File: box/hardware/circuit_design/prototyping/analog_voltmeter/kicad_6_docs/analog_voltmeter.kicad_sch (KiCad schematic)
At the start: 0 parts

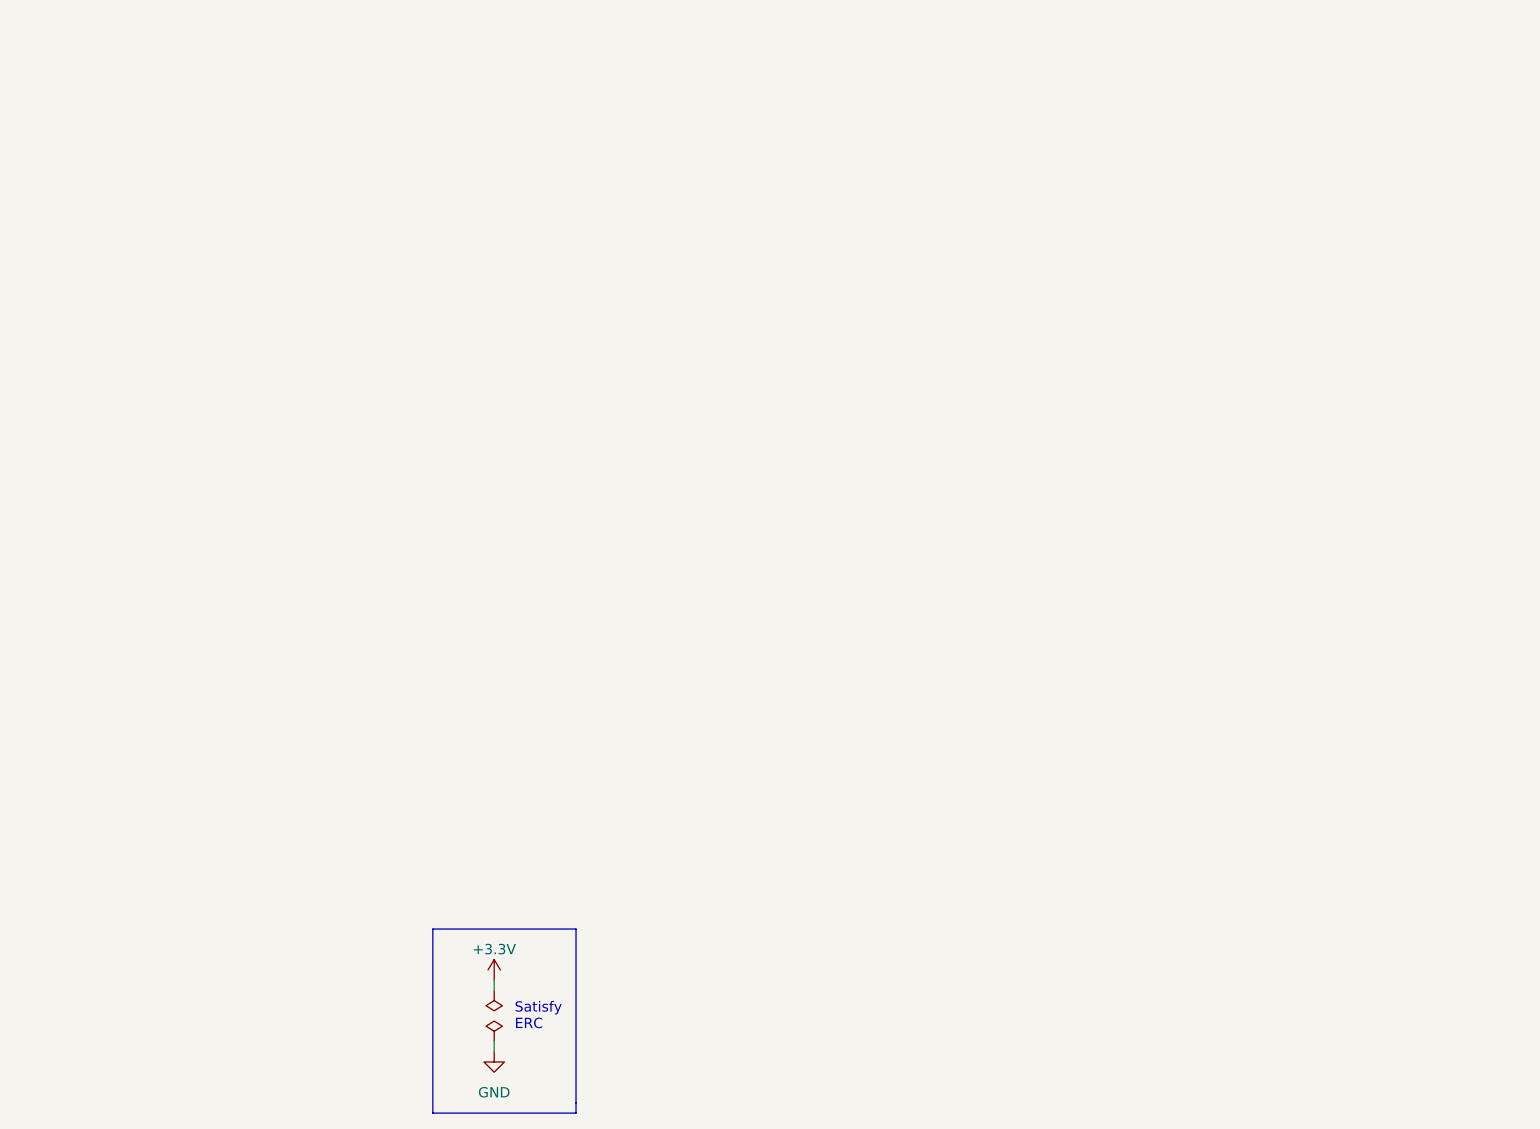
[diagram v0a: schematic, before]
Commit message: Change LED and switch breakouts, use headers instead of components
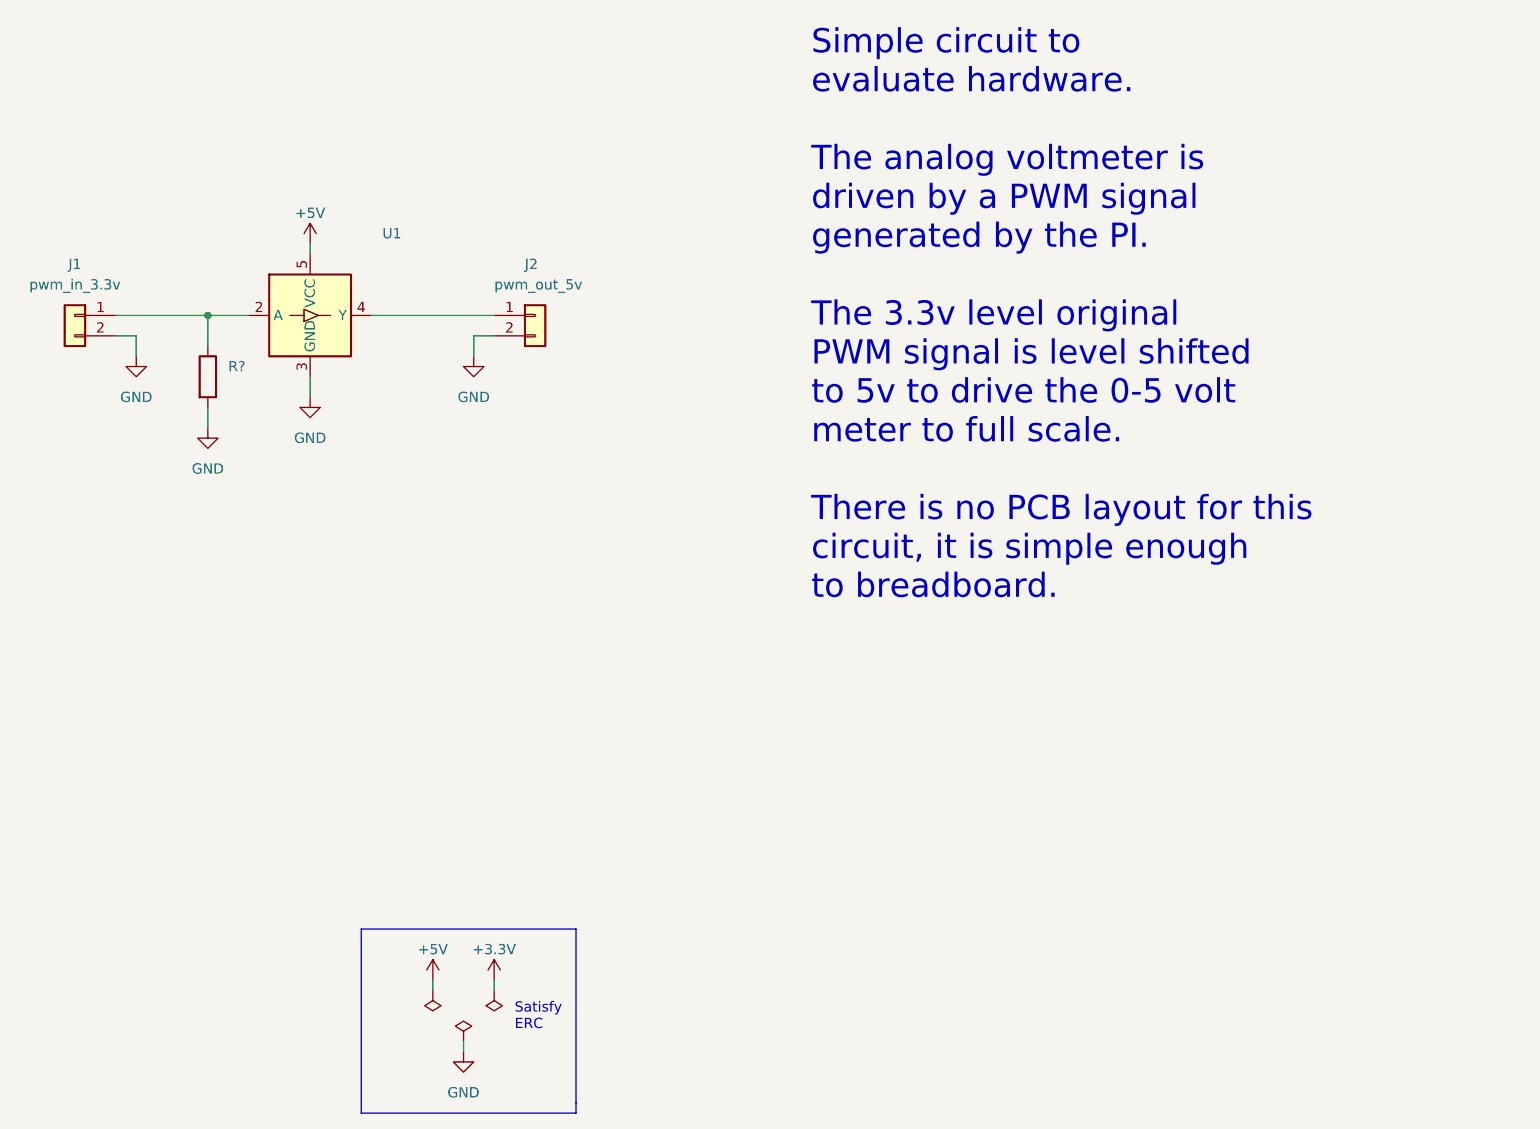
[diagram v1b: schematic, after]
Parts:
- added J1: pwm_in_3.3v, symbol Connector_Generic:Conn_01x02
- added J2: pwm_out_5v, symbol Connector_Generic:Conn_01x02
- added R?: (no value), symbol Device:R
- added U1: (no value), symbol Logic_LevelTranslator:SN74LV1T34DBV
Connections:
- net GND: now also J1.2 (Pin_2), J2.2 (Pin_2), R?.2, U1.3 (GND)
- new net: J2.1 (Pin_1), U1.4 (Y)
- new net: J1.1 (Pin_1), R?.1, U1.2 (A)
- new net +5V: U1.5 (VCC)
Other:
- note added: "Simple circuit to evaluate hardware. The analog voltmeter is driven by a PWM signal generated by the PI. The 3.3v level original PWM signal is level shifted to 5v to drive the 0-5 volt meter to full scale. There is no PCB layout for this circuit, it is simple enough to breadboard."
